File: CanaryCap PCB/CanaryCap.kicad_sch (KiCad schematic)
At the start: 1 part

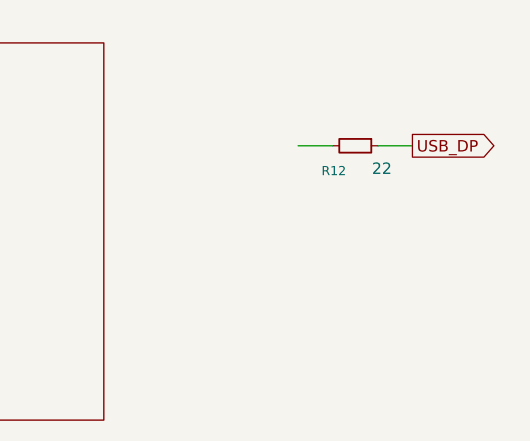
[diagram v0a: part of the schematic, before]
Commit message: Deleted windows blink
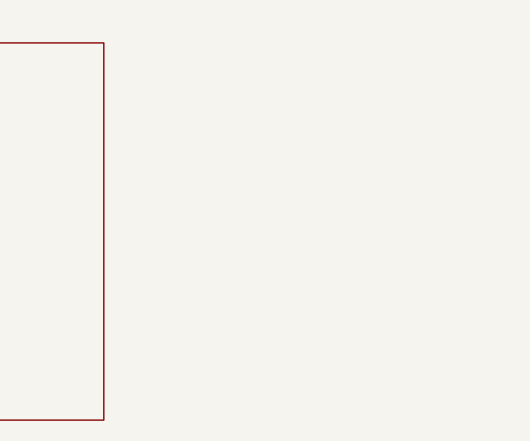
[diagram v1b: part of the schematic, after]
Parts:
- removed R12: 22, Resistor_SMD:R_0603_1608Metric_Pad0.98x0.95mm_HandSolder, symbol Device:R_Small
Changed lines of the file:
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@@
 		(date "2025-10-01")
-	)
-	(wire
-		(pts
-			(xy 193.04 53.34) (xy 196.85 53.34)
-		)
-		(stroke
-			(width 0)
-			(type default)
-		)
-	)
-	(wire
-		(pts
-			(xy 201.93 53.34) (xy 205.74 53.34)
-		)
-		(stroke
-			(width 0)
-			(type default)
-		)
-	)
-	(global_label "USB_DP"
-		(shape output)
-		(at 205.74 53.34 0)
-		(fields_autoplaced yes)
-		(effects
-			(font
-				(size 1.27 1.27)
-			)
-			(justify left)
-		)
-		(property "Intersheetrefs" "${INTERSHEET_REFS}"
-			(at 216.0428 53.34 0)
-			(effects
-				(font
-					(size 1.27 1.27)
-				)
-				(justify left)
-				(hide yes)
-			)
-		)
-	)
-	(symbol
-		(lib_id "Device:R_Small")
-		(at 199.39 53.34 270)
-		(unit 1)
-		(exclude_from_sim no)
-		(in_bom yes)
-		(on_board yes)
-		(dnp no)
-		(property "Reference" "R12"
-			(at 198.374 56.134 90)
-			(effects
-				(font
-					(size 1.016 1.016)
-				)
-				(justify right)
-			)
-		)
-		(property "Value" "22"
-			(at 203.454 55.88 90)
-			(effects
-				(font
-					(size 1.27 1.27)
-				)
-				(justify right)
-			)
-		)
-		(property "Footprint" "Resistor_SMD:R_0603_1608Metric_Pad0.98x0.95mm_HandSolder"
-			(at 199.39 53.34 0)
-			(effects
-				(font
-					(size 1.27 1.27)
-				)
-				(hide yes)
-			)
-		)
-		(property "Datasheet" "~"
-			(at 199.39 53.34 0)
-			(effects
-				(font
-					(size 1.27 1.27)
-				)
-				(hide yes)
-			)
-		)
-		(property "Description" "Resistor, small symbol"
-			(at 199.39 53.34 0)
-			(effects
-				(font
-					(size 1.27 1.27)
-				)
-				(hide yes)
-			)
-		)
-		(pin "2"
-		)
-		(pin "1"
-		)
-		(instances
-			(project "CanaryCap"
-				(path "/406ad30e-b04c-4bb7-9588-aab8ab73084a"
-					(reference "R12")
-					(unit 1)
-				)
-			)
-		)
 	)
 	(sheet
